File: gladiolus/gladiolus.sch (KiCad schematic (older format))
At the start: 138 parts, among them J1 NEIGHBOR1, J2 NEIGHBOR2, J3 Conn_01x02_Female, J7 BONUS_ROW, Q1 Q_NPN_BEC, U1 THS4520RGT, U2 AD8330ARQZ, U3 AD9283, U4 AD9704, U5 LMH6643, U6 74LVC1G3157, U7 74LVC1G3157

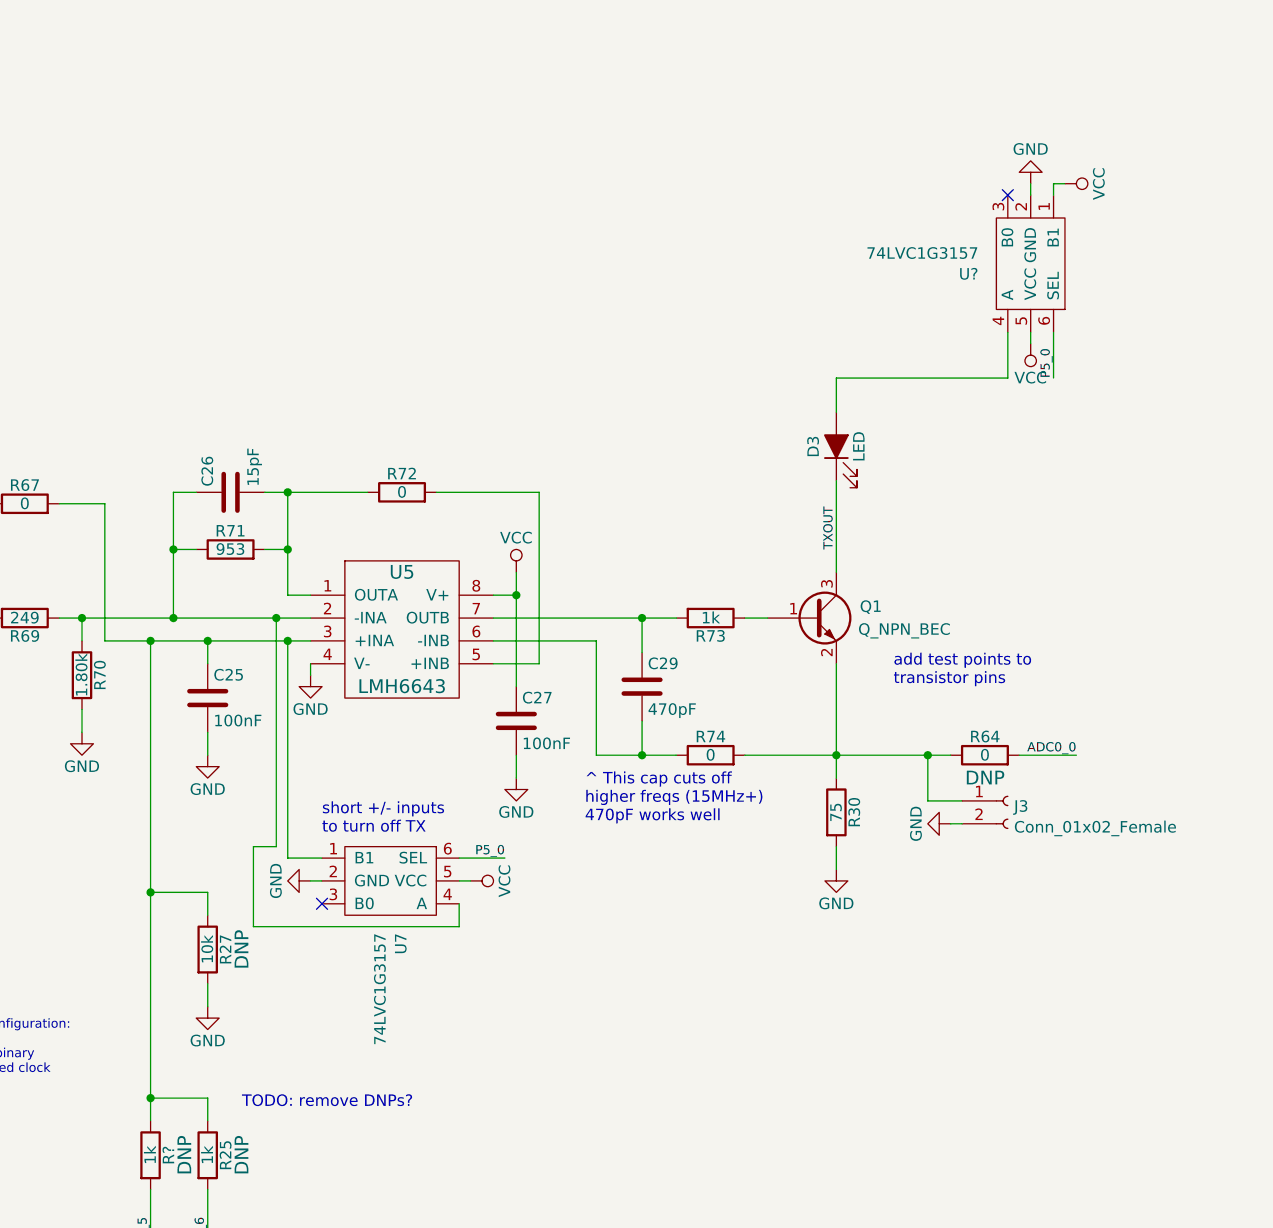
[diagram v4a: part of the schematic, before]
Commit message: Gladiolus: Added design notes. Removed old TX switch and added new TX switch.
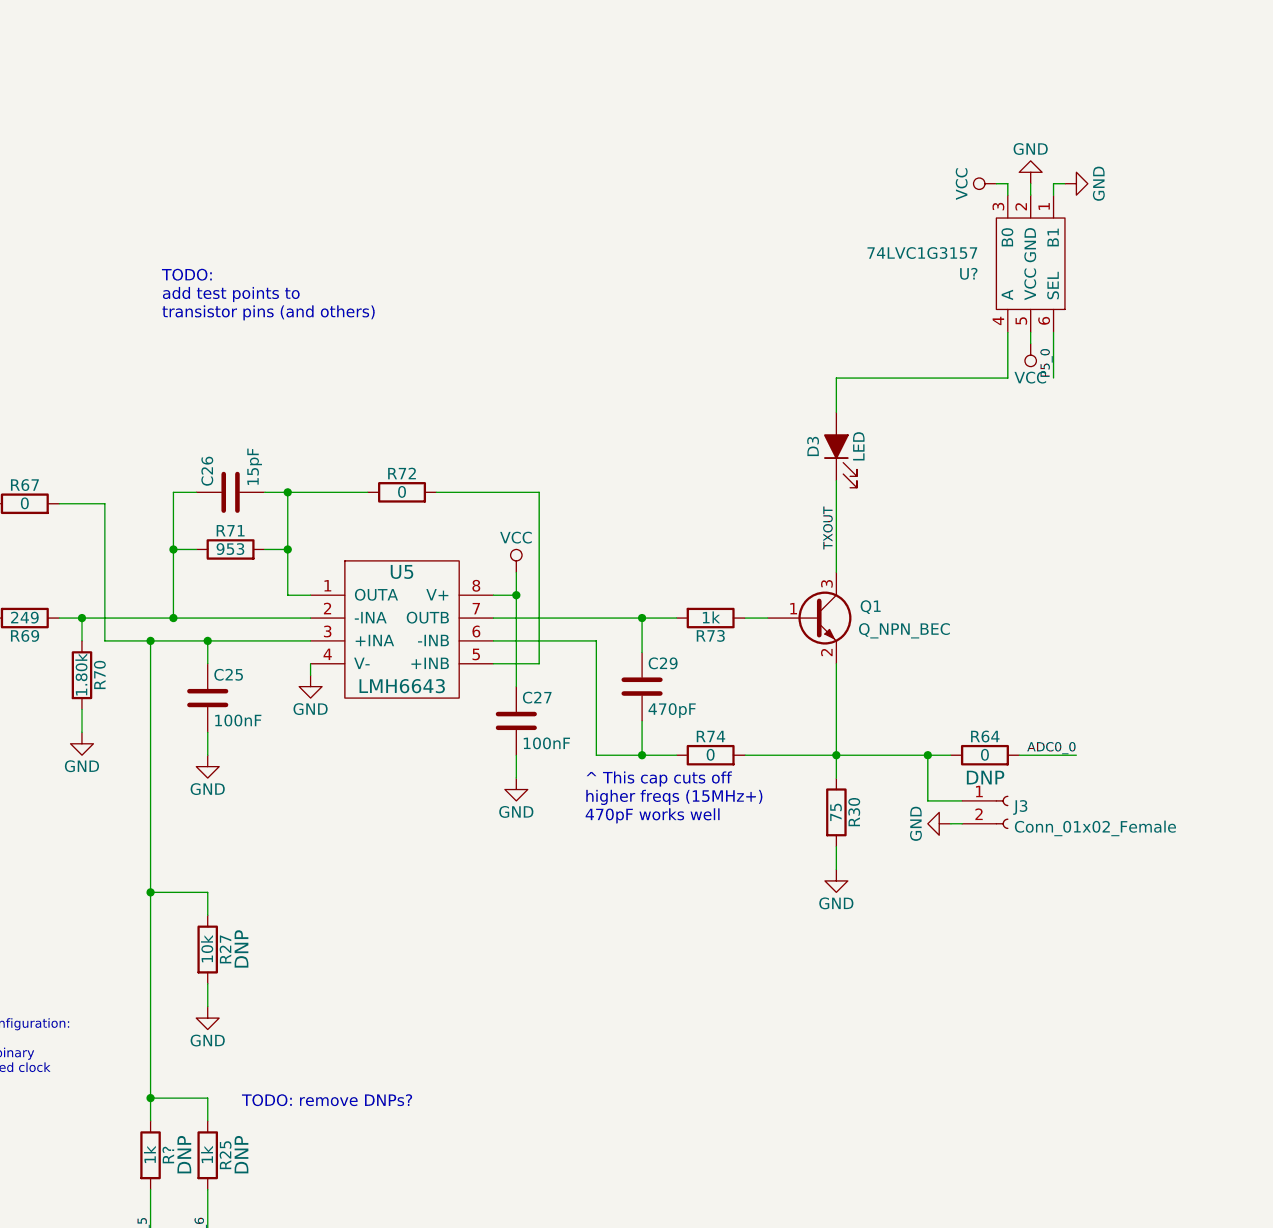
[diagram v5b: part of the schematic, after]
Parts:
- removed U7: 74LVC1G3157, gsg-modules:SOT363, symbol gsg-symbols:74LVC1G3157
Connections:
- net GND: now also U?.1 (B1)
- net VCC: now also U?.3 (B0); no longer U?.1 (B1)
- no-connect marks 64 -> 62
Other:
- note added: "TODO:\nadd test points to\ntransistor pins (and others)"
- note removed: "add test points to\ntransistor pins"
- note removed: "short +/- inputs\nto turn off TX"
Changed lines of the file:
@@
 	5050 7400 5150 7400
-Wire Wire Line
-	6100 7500 6450 7500
-Wire Wire Line
-	5950 7400 6400 7400
 Wire Wire Line
 	3400 6500 3400 6650
@@
 Text Label 1400 2800 1    50   ~ 0
 P2_1
-Text Notes 6600 8350 0    50   ~ 0
-short +/- inputs\nto turn off TX
 $Comp
 L Device:C C29
@@
 	1900 2900 1900 4400
 NoConn ~ 1600 4150
-$Comp
-L gsg-symbols:74LVC1G3157 U7
-U 1 1 5CA8792E
-P 6900 8550
-F 0 "U7" V 6946 8322 50  0000 R CNN
-F 1 "74LVC1G3157" V 6855 8322 50  0000 R CNN
-F 2 "gsg-modules:SOT363" H 6900 8550 50  0001 C CNN
-F 3 "" H 6900 8550 50  0001 C CNN
-F 4 "Diodes Incorporated" V 6855 8322 50  0001 R CNN "Manufacturer"
-F 5 "74LVC1G3157DW-7" H 6900 8550 50  0001 C CNN "Part Number"
-F 6 "IC SWITCH SPDT 6 OHM SOT363" V 6764 8322 50  0001 R CNN "Description"
-	1    6900 8550
-	1    0    0    -1
-$EndComp
-$Comp
-L power:VCC #PWR0106
-U 1 1 5CAEC765
-P 7250 8550
-F 0 "#PWR0106" H 7250 8400 50  0001 C CNN
-F 1 "VCC" H 7250 8700 50  0000 C CNN
-F 2 "" H 7250 8550 60  0000 C CNN
-F 3 "" H 7250 8550 60  0000 C CNN
-	1    7250 8550
-	0    1    1    0
-$EndComp
-Wire Wire Line
-	7200 8550 7250 8550
-$Comp
-L power:GND #PWR0107
-U 1 1 5CB4C675
-P 6550 8550
-F 0 "#PWR0107" H 6550 8300 50  0001 C CNN
-F 1 "GND" H 6550 8400 50  0000 C CNN
-F 2 "" H 6550 8550 50  0000 C CNN
-F 3 "" H 6550 8550 50  0000 C CNN
-	1    6550 8550
-	0    1    1    0
-$EndComp
-Wire Wire Line
-	6550 8550 6600 8550
-Text Label 7400 8450 2    40   ~ 0
-P5_0
-Wire Wire Line
-	7200 8450 7400 8450
 Wire Wire Line
 	6550 7600 6550 7650
-Wire Wire Line
-	6450 7500 6450 8450
-Wire Wire Line
-	6450 8450 6600 8450
-Connection ~ 6450 7500
-Wire Wire Line
-	6450 7500 6550 7500
-NoConn ~ 6600 8650
-Wire Wire Line
-	6400 7400 6400 8400
-Wire Wire Line
-	6400 8400 6300 8400
-Wire Wire Line
-	6300 8400 6300 8750
-Wire Wire Line
-	6300 8750 7200 8750
-Wire Wire Line
-	7200 8750 7200 8650
-Connection ~ 6400 7400
-Wire Wire Line
-	6400 7400 6550 7400
 $Comp
 L Device:R R64
@@
 Wire Wire Line
 	9800 6150 9800 6350
-NoConn ~ 9600 5550
 Wire Wire Line
 	4150 6900 5150 6900
@@
 L power:VCC #PWR?
 U 1 1 5CBE6FDC
+P 9550 5500
+F 0 "#PWR?" H 9550 5350 50  0001 C CNN
+F 1 "VCC" H 9550 5650 50  0000 C CNN
+F 2 "" H 9550 5500 60  0000 C CNN
+F 3 "" H 9550 5500 60  0000 C CNN
+	1    9550 5500
+	0    -1   -1   0
+$EndComp
+Wire Wire Line
+	9850 5500 9800 5500
+Wire Wire Line
+	9800 5500 9800 5550
+Wire Wire Line
+	8850 6800 8850 7200
+Text Notes 5900 6100 0    50   ~ 0
+TODO:\nadd test points to\ntransistor pins (and others)
+$Comp
+L power:GND #PWR?
+U 1 1 5CBF6F0D
 P 9850 5500
-F 0 "#PWR?" H 9850 5350 50  0001 C CNN
-F 1 "VCC" H 9850 5650 50  0000 C CNN
-F 2 "" H 9850 5500 60  0000 C CNN
-F 3 "" H 9850 5500 60  0000 C CNN
+F 0 "#PWR?" H 9850 5250 50  0001 C CNN
+F 1 "GND" H 9850 5350 50  0000 C CNN
+F 2 "" H 9850 5500 50  0000 C CNN
+F 3 "" H 9850 5500 50  0000 C CNN
 	1    9850 5500
-	0    1    1    0
-$EndComp
-Wire Wire Line
-	9850 5500 9800 5500
-Wire Wire Line
-	9800 5500 9800 5550
-Wire Wire Line
-	8850 6800 8850 7200
-Text Notes 9100 7700 0    50   ~ 0
-add test points to\ntransistor pins
+	0    -1   -1   0
+$EndComp
+Wire Wire Line
+	9600 5550 9600 5500
+Wire Wire Line
+	9600 5500 9550 5500
+Wire Wire Line
+	6100 7500 6550 7500
+Wire Wire Line
+	5950 7400 6550 7400
 $EndSCHEMATC

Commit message: Gladiolus: Added test points, switched connections on RV1, moved TX shutoff switch position, changed RX switch control pin from SPIFI pin J2.37
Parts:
- removed J3: Conn_01x02_Female, gsg-modules:HEADER-1x2, symbol Connector:Conn_01x02_Female
- added TP1, TP2, TP3, TP4, TP5, TP6, TP7: TestPoint, gsg-modules:TESTPOINT-50MIL, symbol Connector:TestPoint
- RV1: Note DNP -> (none)
- gave numbers to parts that had none: 2
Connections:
- net GND: now also RV1.3; no longer RV1.1
- net P2_1: now also R77.2; no longer R78.1
- net P3_5: no longer R77.2
- net P6_7: now also R78.1
- net TXOUT: now also TP6.1
- net VCC: now also RV1.1; no longer RV1.3
- net at Q1.2 (E), R30.1, R64.1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: now also TP7.1
- net at Q1.1 (B), R73.1: now also TP5.1
- net at R69.2, U4.20 (IOUTB): now also TP1.1
- net at C26.1, R69.1, R70.1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: now also TP3.1
- net at C25.1, R24.1, R25.1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: now also TP2.1
- net at R72.2, U5.5 (+INB): now also TP4.1
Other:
- note removed: "TODO: remove DNPs?"
- note removed: "TODO:\nadd test points to\ntransistor pins (and others)"
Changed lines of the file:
@@
 Sheet 1 1
 Title "GreatFET Gladiolus"
-Date "2019-02-27"
+Date "2019-04-22"
 Rev ""
 Comp "Copyright 2015 Michael Ossmann"
@@
 L power:VCC #PWR056
 U 1 1 585D3B5E
-P 1950 5100
-F 0 "#PWR056" H 1950 4950 50  0001 C CNN
-F 1 "VCC" H 1950 5250 50  0000 C CNN
-F 2 "" H 1950 5100 60  0000 C CNN
-F 3 "" H 1950 5100 60  0000 C CNN
-	1    1950 5100
-	1    0    0    -1
+P 1950 5600
+F 0 "#PWR056" H 1950 5450 50  0001 C CNN
+F 1 "VCC" H 1950 5750 50  0000 C CNN
+F 2 "" H 1950 5600 60  0000 C CNN
+F 3 "" H 1950 5600 60  0000 C CNN
+	1    1950 5600
+	-1   0    0    1
 $EndComp
 $Comp
 L power:GND #PWR057
 U 1 1 585D3DE9
-P 1950 5600
-F 0 "#PWR057" H 1950 5350 50  0001 C CNN
-F 1 "GND" H 1950 5450 50  0000 C CNN
-F 2 "" H 1950 5600 50  0000 C CNN
-F 3 "" H 1950 5600 50  0000 C CNN
-	1    1950 5600
-	1    0    0    -1
+P 1950 5100
+F 0 "#PWR057" H 1950 4850 50  0001 C CNN
+F 1 "GND" H 1950 4950 50  0000 C CNN
+F 2 "" H 1950 5100 50  0000 C CNN
+F 3 "" H 1950 5100 50  0000 C CNN
+	1    1950 5100
+	-1   0    0    1
 $EndComp
 $Comp
@@
 F 5 "3306F-1-103" H 1950 5350 60  0001 C CNN "Part Number"
 F 6 "10k Ohm 0.2W, 1/5W PC Pins Through Hole Trimmer Potentiometer Cermet 1 Turn Top Adjustment" H 1950 5350 60  0001 C CNN "Description"
-F 7 "DNP" H 1950 5200 60  0000 C CNN "Note"
 	1    1950 5350
 	1    0    0    1
@@
 	2200 3250 2200 3350
 Wire Wire Line
-	8450 7400 8550 7400
+	8450 7400 8500 7400
 Wire Wire Line
 	8850 8400 8850 8500
@@
 	15300 3800 15500 3800
 Wire Wire Line
-	5650 6900 5450 6900
+	5650 6900 5500 6900
 Wire Wire Line
 	4150 6900 4150 7200
@@
 	0    -1   -1   0
 $EndComp
-Text Label 1100 2800 1    50   ~ 0
-P3_5
 Wire Wire Line
 	1500 4150 1500 4200
@@
 	1400 3100 1400 3300
 Connection ~ 1400 3300
-Text Label 1400 2800 1    50   ~ 0
+Text Label 1100 2800 1    50   ~ 0
 P2_1
 $Comp
@@
 	5650 6900 5650 7500
 Wire Wire Line
-	3850 7500 5050 7500
+	3850 7500 4800 7500
 Wire Wire Line
 	3850 7400 4150 7400
@@
 NoConn ~ 15300 2500
 NoConn ~ 15300 2600
-NoConn ~ 15300 2700
 NoConn ~ 15200 3100
 NoConn ~ 16300 3100
@@
 Wire Wire Line
 	8850 8000 9250 8000
-$Comp
-L Connector:Conn_01x02_Female J3
-U 1 1 5C85EBB0
-P 9600 8200
-F 0 "J3" H 9627 8176 50  0000 L CNN
-F 1 "Conn_01x02_Female" H 9627 8085 50  0000 L CNN
-F 2 "gsg-modules:HEADER-1x2" H 9600 8200 50  0001 C CNN
-F 3 "~" H 9600 8200 50  0001 C CNN
-F 4 "DNP" H 9600 8200 50  0001 C CNN "Note"
-	1    9600 8200
-	1    0    0    -1
-$EndComp
-Wire Wire Line
-	9250 8000 9250 8200
-Wire Wire Line
-	9250 8200 9400 8200
 Connection ~ 9250 8000
 Wire Wire Line
 	9250 8000 9350 8000
-$Comp
-L power:GND #PWR0108
-U 1 1 5C8BF1A4
-P 9350 8300
-F 0 "#PWR0108" H 9350 8050 50  0001 C CNN
-F 1 "GND" H 9350 8150 50  0000 C CNN
-F 2 "" H 9350 8300 50  0000 C CNN
-F 3 "" H 9350 8300 50  0000 C CNN
-	1    9350 8300
-	0    1    1    0
-$EndComp
-Wire Wire Line
-	9350 8300 9400 8300
 Wire Wire Line
 	8850 6500 8850 6350
@@
 	15800 3450 16100 3450
 $Comp
-L gsg-symbols:74LVC1G3157 U?
+L gsg-symbols:74LVC1G3157 U7
 U 1 1 5CB72BB9
 P 9700 5850
-F 0 "U?" V 9746 5622 50  0000 R CNN
+F 0 "U7" V 9746 5622 50  0000 R CNN
 F 1 "74LVC1G3157" V 9655 5622 50  0000 R CNN
 F 2 "gsg-modules:SOT363" H 9700 5850 50  0001 C CNN
@@
 $EndComp
 $Comp
-L power:VCC #PWR?
+L power:VCC #PWR0106
 U 1 1 5CB72BC0
 P 9700 6200
-F 0 "#PWR?" H 9700 6050 50  0001 C CNN
+F 0 "#PWR0106" H 9700 6050 50  0001 C CNN
 F 1 "VCC" H 9700 6350 50  0000 C CNN
 F 2 "" H 9700 6200 60  0000 C CNN
@@
 	9700 6150 9700 6200
 $Comp
-L power:GND #PWR?
+L power:GND #PWR0107
 U 1 1 5CB72BC7
 P 9700 5500
-F 0 "#PWR?" H 9700 5250 50  0001 C CNN
+F 0 "#PWR0107" H 9700 5250 50  0001 C CNN
 F 1 "GND" H 9700 5350 50  0000 C CNN
 F 2 "" H 9700 5500 50  0000 C CNN
@@
 	9600 6350 8850 6350
 $Comp
-L Device:R R?
+L Device:R R24
 U 1 1 5CB7D036
 P 5850 9750
-F 0 "R?" V 5930 9750 50  0000 C CNN
+F 0 "R24" V 5930 9750 50  0000 C CNN
 F 1 "1k" V 5850 9750 50  0000 C CNN
 F 2 "gsg-modules:0603" V 5780 9750 50  0001 C CNN
@@
 	1    0    0    -1
 $EndComp
-Text Notes 6250 9550 0    50   ~ 0
-TODO: remove DNPs?
 Wire Wire Line
-	7100 6850 7550 6850
+	7100 6850 7300 6850
 $Comp
-L power:VCC #PWR?
+L power:VCC #PWR0108
 U 1 1 5CBE6FDC
 P 9550 5500
-F 0 "#PWR?" H 9550 5350 50  0001 C CNN
+F 0 "#PWR0108" H 9550 5350 50  0001 C CNN
 F 1 "VCC" H 9550 5650 50  0000 C CNN
 F 2 "" H 9550 5500 60  0000 C CNN
@@
 Wire Wire Line
 	9800 5500 9800 5550
-Wire Wire Line
-	8850 6800 8850 7200
-Text Notes 5900 6100 0    50   ~ 0
-TODO:\nadd test points to\ntransistor pins (and others)
 $Comp
-L power:GND #PWR?
+L power:GND #PWR0109
 U 1 1 5CBF6F0D
 P 9850 5500
-F 0 "#PWR?" H 9850 5250 50  0001 C CNN
+F 0 "#PWR0109" H 9850 5250 50  0001 C CNN
 F 1 "GND" H 9850 5350 50  0000 C CNN
 F 2 "" H 9850 5500 50  0000 C CNN
@@
 	6100 7500 6550 7500
 Wire Wire Line
-	5950 7400 6550 7400
+	5950 7400 6000 7400
+Text Label 1400 2800 1    40   ~ 0
+P6_7
+NoConn ~ 15300 3000
+$Comp
+L Connector:TestPoint TP7
+U 1 1 5CCC58CD
+P 9250 7800
+F 0 "TP7" H 9308 7920 50  0000 L CNN
+F 1 "TestPoint" H 9308 7829 50  0000 L CNN
+F 2 "gsg-modules:TESTPOINT-50MIL" H 9450 7800 50  0001 C CNN
+F 3 "~" H 9450 7800 50  0001 C CNN
+	1    9250 7800
+	1    0    0    -1
+$EndComp
+Wire Wire Line
+	9250 7800 9250 8000
+Wire Wire Line
+	8850 6800 8850 7150
+Wire Wire Line
+	8850 7150 8950 7150
+Connection ~ 8850 7150
+Wire Wire Line
+	8850 7150 8850 7200
+$Comp
+L Connector:TestPoint TP6
+U 1 1 5CDE186E
+P 8950 7150
+F 0 "TP6" V 8904 7338 50  0000 L CNN
+F 1 "TestPoint" V 8995 7338 50  0000 L CNN
+F 2 "gsg-modules:TESTPOINT-50MIL" H 9150 7150 50  0001 C CNN
+F 3 "~" H 9150 7150 50  0001 C CNN
+	1    8950 7150
+	0    1    1    0
+$EndComp
+$Comp
+L Connector:TestPoint TP5
+U 1 1 5CDE1A4D
+P 8250 7200
+F 0 "TP5" H 8308 7320 50  0000 L CNN
+F 1 "TestPoint" H 8308 7229 50  0000 L CNN
+F 2 "gsg-modules:TESTPOINT-50MIL" H 8450 7200 50  0001 C CNN
+F 3 "~" H 8450 7200 50  0001 C CNN
+	1    8250 7200
+	1    0    0    -1
+$EndComp
+Wire Wire Line
+	8250 7200 8250 7250
+Wire Wire Line
+	8250 7250 8500 7250
+Wire Wire Line
+	8500 7250 8500 7400
+Connection ~ 8500 7400
+Wire Wire Line
+	8500 7400 8550 7400
+$Comp
+L Connector:TestPoint TP4
+U 1 1 5CE408DE
+P 7300 6800
+F 0 "TP4" H 7358 6920 50  0000 L CNN
+F 1 "TestPoint" H 7358 6829 50  0000 L CNN
+F 2 "gsg-modules:TESTPOINT-50MIL" H 7500 6800 50  0001 C CNN
+F 3 "~" H 7500 6800 50  0001 C CNN
+	1    7300 6800
+	1    0    0    -1
+$EndComp
+Wire Wire Line
+	7300 6800 7300 6850
+Connection ~ 7300 6850
+Wire Wire Line
+	7300 6850 7550 6850
+$Comp
+L Connector:TestPoint TP2
+U 1 1 5CEA08FF
+P 5500 6850
+F 0 "TP2" H 5558 6970 50  0000 L CNN
+F 1 "TestPoint" H 5558 6879 50  0000 L CNN
+F 2 "gsg-modules:TESTPOINT-50MIL" H 5700 6850 50  0001 C CNN
+F 3 "~" H 5700 6850 50  0001 C CNN
+	1    5500 6850
+	1    0    0    -1
+$EndComp
+Wire Wire Line
+	5500 6850 5500 6900
+Connection ~ 5500 6900
+Wire Wire Line
+	5500 6900 5450 6900
+$Comp
+L Connector:TestPoint TP3
+U 1 1 5CF024CE
+P 6000 7350
+F 0 "TP3" H 6058 7470 50  0000 L CNN
+F 1 "TestPoint" H 6058 7379 50  0000 L CNN
+F 2 "gsg-modules:TESTPOINT-50MIL" H 6200 7350 50  0001 C CNN
+F 3 "~" H 6200 7350 50  0001 C CNN
+	1    6000 7350
+	1    0    0    -1
+$EndComp
+Wire Wire Line
+	6000 7350 6000 7400
+Connection ~ 6000 7400
+Wire Wire Line
+	6000 7400 6550 7400
+$Comp
+L Connector:TestPoint TP1
+U 1 1 5CF63767
+P 4800 7550
+F 0 "TP1" H 4742 7577 50  0000 R CNN
+F 1 "TestPoint" H 4742 7668 50  0000 R CNN
+F 2 "gsg-modules:TESTPOINT-50MIL" H 5000 7550 50  0001 C CNN
+F 3 "~" H 5000 7550 50  0001 C CNN
+	1    4800 7550
+	-1   0    0    1
+$EndComp
+Wire Wire Line
+	4800 7550 4800 7500
+Connection ~ 4800 7500
+Wire Wire Line
+	4800 7500 5050 7500
 $EndSCHEMATC
